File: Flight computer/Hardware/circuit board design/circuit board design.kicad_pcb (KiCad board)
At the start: 4 copper layers, 91 parts, among them J1 Conn_01x04, J2 Conn_01x02, J3 Conn_01x02, Q1 Q_PMOS_DGS, U10 BMI088, U11 ATSAML21J18B-MUT, U12 MAX2659ELT+, U13 SAFEB1G57KE0F00, U2 AS179-92LF, U3 Si4463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

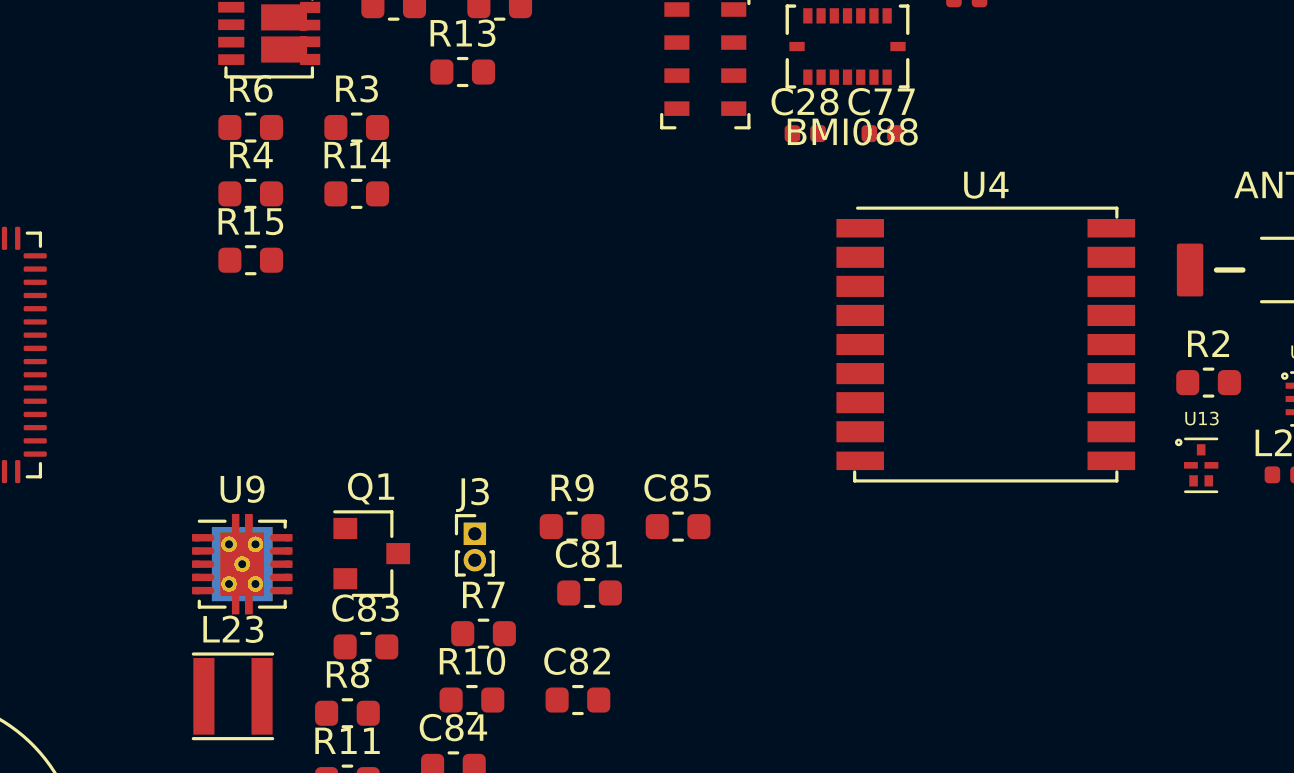
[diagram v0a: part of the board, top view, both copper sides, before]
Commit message: more upgrades
- removed the comparators
- added the cost and link to buy components
- added in a symbol for USB
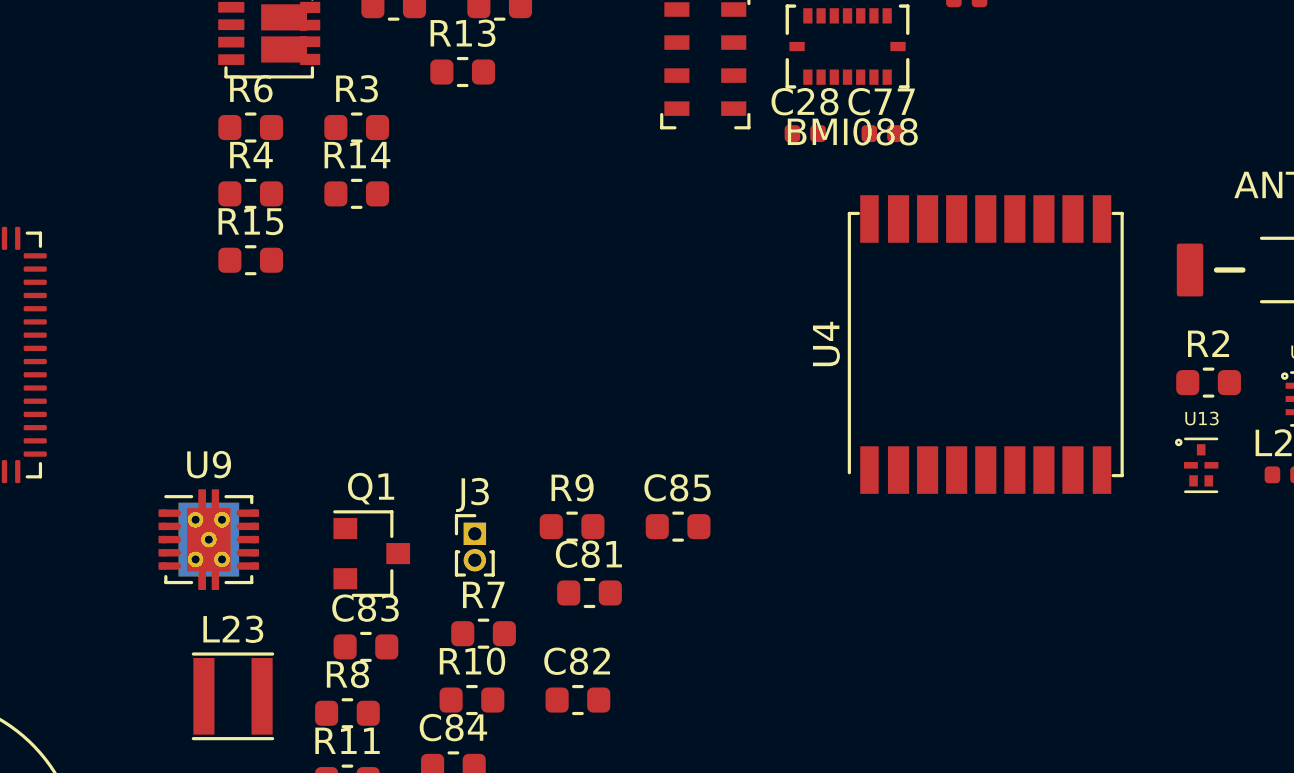
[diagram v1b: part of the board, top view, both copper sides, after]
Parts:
- moved U9 1.57 mm to (157.0, 97.2)
- turned U4 to 90 degrees
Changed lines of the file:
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@@
     (solder_mask_min_width 0.25)
     (aux_axis_origin 0 0)
-    (visible_elements FFFFFF7F)
+    (visible_elements 7FFFFFFF)
     (pcbplotparams
       (layerselection 0x010fc_ffffffff)
@@
   )
   (module RF_GPS:ublox_MAX (layer F.Cu)
-    (at 186.425001 89.775001)
+    (at 186.425001 89.775001 90)
     (descr "ublox MAX 6/7/8, (https://www.u-blox.com/sites/default/files/MAX-8-M8-FW3_HardwareIntegrationManual_%28UBX-15030059%29.pdf)")
     (tags "GPS ublox MAX 6/7/8")
     (attr smd)
-    (fp_text reference U4 (at 0 -6) (layer F.SilkS)
+    (fp_text reference U4 (at 0 -6 90) (layer F.SilkS)
       (effects (font (size 1 1) (thickness 0.15)))
     )
-    (fp_text value MAX-M8C (at 0 1.5) (layer F.Fab)
+    (fp_text value MAX-M8C (at 0 1.5 90) (layer F.Fab)
       (effects (font (size 1 1) (thickness 0.15)))
     )
-    (fp_text user %R (at 0 0) (layer F.Fab)
+    (fp_text user %R (at 0 0 90) (layer F.Fab)
       (effects (font (size 1 1) (thickness 0.15)))
     )
@@
     (fp_line (start -3.85 -4.4) (end -4.85 -4.05) (layer F.Fab) (width 0.1))
     (fp_line (start -4.85 -4.75) (end -3.85 -4.4) (layer F.Fab) (width 0.1))
-    (pad 1 smd rect (at -4.75 -4.4) (size 1.8 0.7) (layers F.Cu F.Paste F.Mask)
+    (pad 1 smd rect (at -4.75 -4.4 90) (size 1.8 0.7) (layers F.Cu F.Paste F.Mask)
       (net 3 GND))
-    (pad 2 smd rect (at -4.75 -3.3) (size 1.8 0.8) (layers F.Cu F.Paste F.Mask)
+    (pad 2 smd rect (at -4.75 -3.3 90) (size 1.8 0.8) (layers F.Cu F.Paste F.Mask)
       (net 59 /gps/GPS_TXD))
-    (pad 3 smd rect (at -4.75 -2.2) (size 1.8 0.8) (layers F.Cu F.Paste F.Mask)
+    (pad 3 smd rect (at -4.75 -2.2 90) (size 1.8 0.8) (layers F.Cu F.Paste F.Mask)
       (net 60 /gps/GPS_RXD))
-    (pad 4 smd rect (at -4.75 -1.1) (size 1.8 0.8) (layers F.Cu F.Paste F.Mask)
+    (pad 4 smd rect (at -4.75 -1.1 90) (size 1.8 0.8) (layers F.Cu F.Paste F.Mask)
       (net 61 /gps/GPS_1PPS))
-    (pad 5 smd rect (at -4.75 0) (size 1.8 0.8) (layers F.Cu F.Paste F.Mask))
-    (pad 6 smd rect (at -4.75 1.1) (size 1.8 0.8) (layers F.Cu F.Paste F.Mask))
-    (pad 7 smd rect (at -4.75 2.2) (size 1.8 0.8) (layers F.Cu F.Paste F.Mask))
-    (pad 8 smd rect (at -4.75 3.3) (size 1.8 0.8) (layers F.Cu F.Paste F.Mask)
+    (pad 5 smd rect (at -4.75 0 90) (size 1.8 0.8) (layers F.Cu F.Paste F.Mask))
+    (pad 6 smd rect (at -4.75 1.1 90) (size 1.8 0.8) (layers F.Cu F.Paste F.Mask))
+    (pad 7 smd rect (at -4.75 2.2 90) (size 1.8 0.8) (layers F.Cu F.Paste F.Mask))
+    (pad 8 smd rect (at -4.75 3.3 90) (size 1.8 0.8) (layers F.Cu F.Paste F.Mask)
       (net 5 +3V3))
-    (pad 9 smd rect (at -4.75 4.4) (size 1.8 0.7) (layers F.Cu F.Paste F.Mask)
+    (pad 9 smd rect (at -4.75 4.4 90) (size 1.8 0.7) (layers F.Cu F.Paste F.Mask)
       (net 62 /gps/GPS_NRES))
-    (pad 10 smd rect (at 4.75 4.4) (size 1.8 0.7) (layers F.Cu F.Paste F.Mask)
+    (pad 10 smd rect (at 4.75 4.4 90) (size 1.8 0.7) (layers F.Cu F.Paste F.Mask)
       (net 3 GND))
-    (pad 11 smd rect (at 4.75 3.3) (size 1.8 0.8) (layers F.Cu F.Paste F.Mask)
+    (pad 11 smd rect (at 4.75 3.3 90) (size 1.8 0.8) (layers F.Cu F.Paste F.Mask)
       (net 63 "Net-(U13-Pad4)"))
-    (pad 12 smd rect (at 4.75 2.2) (size 1.8 0.8) (layers F.Cu F.Paste F.Mask)
+    (pad 12 smd rect (at 4.75 2.2 90) (size 1.8 0.8) (layers F.Cu F.Paste F.Mask)
       (net 3 GND))
-    (pad 13 smd rect (at 4.75 1.1) (size 1.8 0.8) (layers F.Cu F.Paste F.Mask)
+    (pad 13 smd rect (at 4.75 1.1 90) (size 1.8 0.8) (layers F.Cu F.Paste F.Mask)
       (net 41 "Net-(R2-Pad1)"))
-    (pad 14 smd rect (at 4.75 0) (size 1.8 0.8) (layers F.Cu F.Paste F.Mask)
+    (pad 14 smd rect (at 4.75 0 90) (size 1.8 0.8) (layers F.Cu F.Paste F.Mask)
       (net 64 "Net-(U12-Pad4)"))
-    (pad 15 smd rect (at 4.75 -1.1) (size 1.8 0.8) (layers F.Cu F.Paste F.Mask))
-    (pad 16 smd rect (at 4.75 -2.2) (size 1.8 0.8) (layers F.Cu F.Paste F.Mask)
+    (pad 15 smd rect (at 4.75 -1.1 90) (size 1.8 0.8) (layers F.Cu F.Paste F.Mask))
+    (pad 16 smd rect (at 4.75 -2.2 90) (size 1.8 0.8) (layers F.Cu F.Paste F.Mask)
       (net 65 /gps/GPS_SDA))
-    (pad 17 smd rect (at 4.75 -3.3) (size 1.8 0.8) (layers F.Cu F.Paste F.Mask)
+    (pad 17 smd rect (at 4.75 -3.3 90) (size 1.8 0.8) (layers F.Cu F.Paste F.Mask)
       (net 66 /gps/GPS_SCL))
-    (pad 18 smd rect (at 4.75 -4.4) (size 1.8 0.7) (layers F.Cu F.Paste F.Mask)
+    (pad 18 smd rect (at 4.75 -4.4 90) (size 1.8 0.7) (layers F.Cu F.Paste F.Mask)
       (net 67 /gps/GPS_NSAFEBOOT))
     (model ${KISYS3DMOD}/RF_GPS.3dshapes/ublox_MAX.wrl
@@
   )
   (module Package_SON:Texas_S-PVSON-N10_ThermalVias (layer F.Cu)
-    (at 158.295001 98.085001)
+    (at 157.03 97.155)
     (descr "3x3mm Body, 0.5mm Pitch, S-PVSON-N10, DRC, http://www.ti.com/lit/ds/symlink/tps61201.pdf")
     (tags "0.5 S-PVSON-N10 DRC")

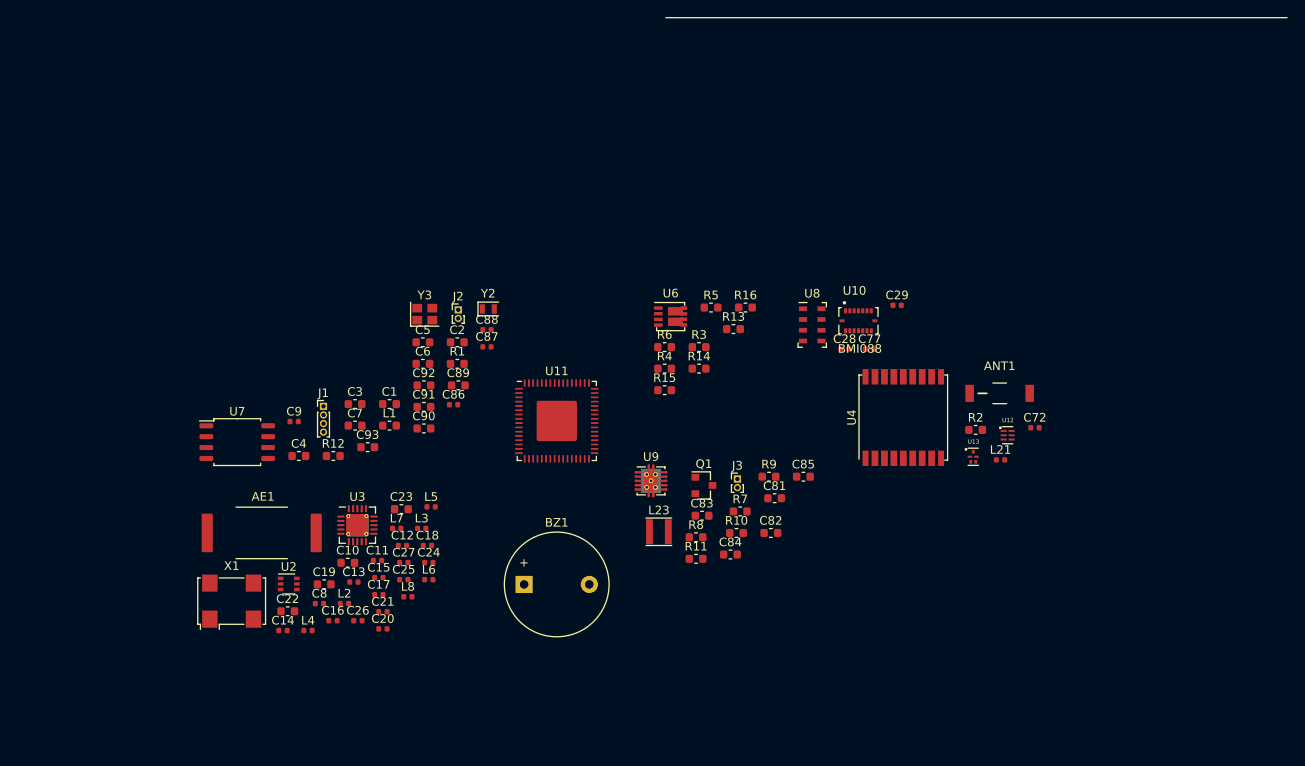
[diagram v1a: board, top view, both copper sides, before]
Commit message: fixed errors with symbol and footprint connections
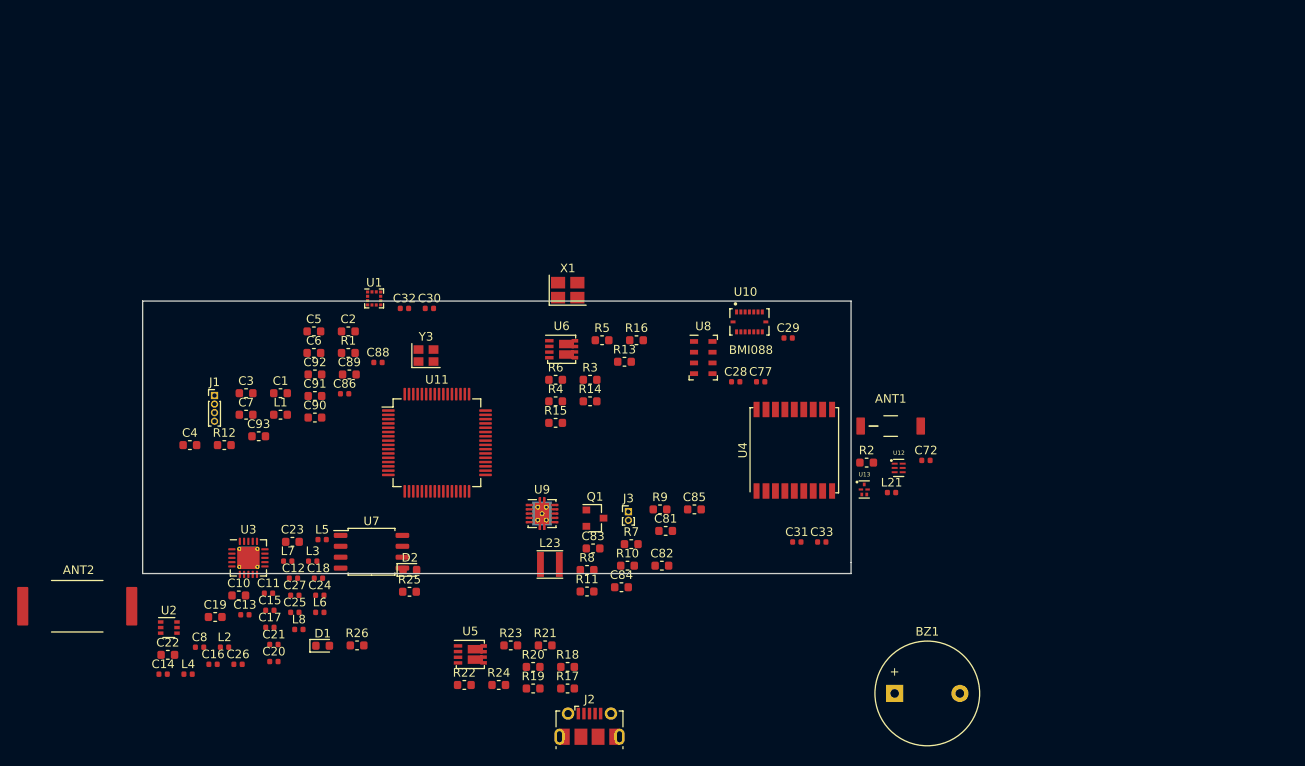
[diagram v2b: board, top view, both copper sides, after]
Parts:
- removed C87, C9: 22pF, Capacitor_SMD:C_0402_1005Metric
- removed Y2: 32.768KHz, Crystal:Crystal_SMD_2012-2Pin_2.0x1.2mm
- added C30: 220nF, Capacitor_SMD:C_0402_1005Metric, F.Cu at (131.2, 77.1)
- added C31: 100nF, Capacitor_SMD:C_0402_1005Metric, F.Cu at (174.0, 104.3)
- added C32: 10uF, Capacitor_SMD:C_0402_1005Metric, F.Cu at (128.3, 77.1)
- added C33: 100nF, Capacitor_SMD:C_0402_1005Metric, F.Cu at (176.9, 104.3)
- added D1: LED, LED_SMD:LED_0603_1608Metric, F.Cu at (118.8, 116.4)
- added D2: LED, LED_SMD:LED_0603_1608Metric, F.Cu at (128.9, 107.5)
- added R17: 3.3K, Resistor_SMD:R_0603_1608Metric, F.Cu at (147.3, 121.3)
- added R18: 3.3K, Resistor_SMD:R_0603_1608Metric, F.Cu at (147.3, 118.8)
- added R19: 100, Resistor_SMD:R_0603_1608Metric, F.Cu at (143.3, 121.3)
- added R20: 100, Resistor_SMD:R_0603_1608Metric, F.Cu at (143.3, 118.8)
- added R21: 100K, Resistor_SMD:R_0603_1608Metric, F.Cu at (144.7, 116.3)
- added R22: 100K, Resistor_SMD:R_0603_1608Metric, F.Cu at (135.3, 120.9)
- added R23: 27K, Resistor_SMD:R_0603_1608Metric, F.Cu at (140.7, 116.3)
- added R24: 27K, Resistor_SMD:R_0603_1608Metric, F.Cu at (139.3, 120.9)
- added R25: 1k, Resistor_SMD:R_0603_1608Metric, F.Cu at (128.9, 110.1)
- added R26: 1k, Resistor_SMD:R_0603_1608Metric, F.Cu at (122.8, 116.3)
- added U1: IIS2MDC, Package_LGA:LGA-12_2x2mm_P0.5mm, F.Cu at (124.8, 75.9)
- added U5: Si7232DN, Package_SO:Vishay_PowerPAK_1212-8_Dual, F.Cu at (136.0, 117.4)
- ANT2: renamed from AE1; value Antenna -> Yageo434
- J2: value Conn_01x02 -> USB_B_Micro; footprint Connector_PinHeader_1.00mm:PinHeader_1x02_P1.00mm_Vertical -> Connector_USB:USB_Micro-B_Molex-105017-0001
- U10: footprint flight-computer:PQFN50P450X300X100-16N -> BMI088:PQFN50P450X300X100-16N
- U11: value ATSAML21J18B-MUT -> ATSAML21J18B-AUT; footprint Package_DFN_QFN:QFN-64-1EP_9x9mm_P0.5mm_EP4.7x4.7mm -> Package_QFP:TQFP-64_10x10mm_P0.5mm
- X1: value 32MHz TCXO -> TM-32.000-AF3-33-S-Oscillator; footprint Oscillator:Oscillator_SMD_IQD_IQXO70-4Pin_7.5x5.0mm -> Oscillator:Oscillator_SMD_SeikoEpson_SG210-4Pin_2.5x2.0mm_HandSoldering
- moved X1 53.3 mm to (147.3, 74.9)
- moved J2 50.9 mm to (149.9, 125.7)
- moved BZ1 45.0 mm to (185.4, 121.9)
- moved ANT2 23.1 mm to (90.2, 111.8)
- moved U7 20.2 mm to (124.5, 105.4)
- moved C14 14.9 mm to (100.2, 119.7)
- moved C16 14.9 mm to (106.0, 118.5)
- moved C22 14.9 mm to (100.7, 117.4)
- moved C26 14.9 mm to (108.9, 118.5)
- moved C8 14.9 mm to (104.4, 116.5)
- moved L2 14.9 mm to (107.3, 116.5)
- moved L4 14.9 mm to (103.1, 119.7)
- moved U2 14.9 mm to (100.8, 114.2)
- moved U11 14.2 mm to (132.1, 92.7)
- moved C72 13.3 mm to (189.1, 94.8)
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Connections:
- net /MCU/USB_DP renamed /power_supply/USB_DM
- ANT1 pad 2: (no net) -> Net-(ANT1-Pad2)
- ANT2 pad 2: (no net) -> Net-(ANT2-Pad2)
- BZ1 pad 1: Net-(BZ1-Pad1) -> /MCU/MCU_PB12
- J2 pad 1: /MCU/USB_DM -> Net-(J2-Pad1)
- R15 pad 1: /MCU/MCU_PA06 -> /MCU/MCU_PB05
- R16 pad 1: /MCU/MCU_PA06 -> /MCU/MCU_PB05
- R5 pad 1: /MCU/MCU_PA05 -> /MCU/MCU_PB04
- R5 pad 2: (no net) -> /pyro_driver/FET_A
- R6 pad 1: /MCU/MCU_PA05 -> /MCU/MCU_PB04
- U10 pad 1: (no net) -> Net-(U10-Pad1)
- U10 pad 13: (no net) -> Net-(U10-Pad13)
- U10 pad 5: (no net) -> Net-(U10-Pad5)
- U11 pad 1: /MCU/XIN32 -> Net-(U11-Pad1)
- U11 pad 10: /gps/GPS_NSAFEBOOT -> /MCU/MCU_PB07
- U11 pad 11: /gps/GPS_NRES -> /gps/GPS_1PPS
- U11 pad 12: /gps/GPS_1PPS -> /MCU/MCU_NSEL4
- U11 pad 13: /sensors/GYRO_RDY -> Net-(U11-Pad13)
- U11 pad 14: /MCU/MCU_PA05 -> /sensors/ACCL_RDY
- U11 pad 15: /MCU/MCU_PA06 -> /sensors/GYRO_RDY
- U11 pad 16: /pyro_driver/FIRE_A -> /sensors/MAG_RDY
- U11 pad 17: /pyro_driver/FIRE_B -> Net-(U11-Pad17)
- U11 pad 2: /MCU/XOUT32 -> Net-(U11-Pad2)
- U11 pad 23: /MCU/MCU_NSEL4 -> /MCU/MCU_MOSI4
- U11 pad 24: /MCU/MCU_MOSI4 -> /MCU/MCU_SCLK4
- U11 pad 25: /MCU/MCU_SCLK4 -> /MCU/MCU_PB12
- U11 pad 26: Net-(BZ1-Pad1) -> /pyro_driver/FIRE_A
- U11 pad 27: (no net) -> /pyro_driver/FIRE_B
- U11 pad 28: (no net) -> /pyro_driver/FIRE_C
- U11 pad 39: (no net) -> /pyro_driver/FIRE_D
- U11 pad 4: /sensors/ACCL_RDY -> Net-(U11-Pad4)
- U11 pad 40: (no net) -> Net-(U11-Pad40)
- U11 pad 49: (no net) -> /MCU/LED_RED
- U11 pad 5: (no net) -> /MCU/MCU_PB04
- U11 pad 50: (no net) -> /MCU/LED_BLUE
- U11 pad 55: (no net) -> Net-(U11-Pad55)
- U11 pad 59: (no net) -> Net-(U11-Pad59)
- U11 pad 6: (no net) -> /MCU/MCU_PB05
- U11 pad 60: (no net) -> Net-(U11-Pad60)
- U11 pad 61: (no net) -> Net-(U11-Pad61)
- U11 pad 62: (no net) -> Net-(U11-Pad62)
- U11 pad 63: (no net) -> /gps/GPS_NRES
- U11 pad 64: (no net) -> /gps/GPS_NSAFEBOOT
- U11 pad 9: (no net) -> /MCU/MCU_PB06
- U3 pad 16: (no net) -> Net-(U3-Pad16)
- U3 pad 5: (no net) -> Net-(U3-Pad5)
- U3 pad 7: (no net) -> Net-(U3-Pad7)
- U4 pad 15: (no net) -> Net-(U4-Pad15)
- U4 pad 5: (no net) -> Net-(U4-Pad5)
- U4 pad 6: (no net) -> Net-(U4-Pad6)
- U4 pad 7: (no net) -> +3V3
- U6 pad 6: /pyro_driver/FET_B -> /pyro_driver/FET_A
- U8 pad 6: (no net) -> Net-(U8-Pad6)
- X1 pad 1: (no net) -> Net-(X1-Pad1)
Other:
- board outline added: 82.5 x 31.8 mm
